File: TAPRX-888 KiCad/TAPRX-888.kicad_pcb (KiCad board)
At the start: 6 copper layers, 76 x 100 mm, 214 parts, among them J1 CONN_SMA_JACK_RA, J10 U.FL-R, J2 CONN_SMA_JACK_RA, J3 CONN_SMA_JACK_RA, J4 CONN_SMA_JACK_RA, J5 USB-3.0, J6 Conn_01x03, J7 Conn_01x03, J8 Conn_01x03, J9 Conn_01x03, Q1 PMOS Si2343DS, Q2 MMBT3904, U1 AP2114H-3.3TRG1, U10 XO-19.2MHZ, U11 CYUSB3014-BZXCT, U14 LP5907MFX-3.3, U16 TLV3501, U18 NC7SV157, U19 74LVC2G14, U2 AP2114H-3.3TRG1, U20 Si5351A, U21 NC7SV157, U22 SN65LVDS1, U3 AP2114H-3.3TRG1, U4 LP5907MFX-3.3, U5 UMW AMS1117-1.2, U6 AD8370, U7 TVS-SP3011, U8 LTC2208CUP_PBF, U9 MX25L3233FM2I, X1 TCXO-27M

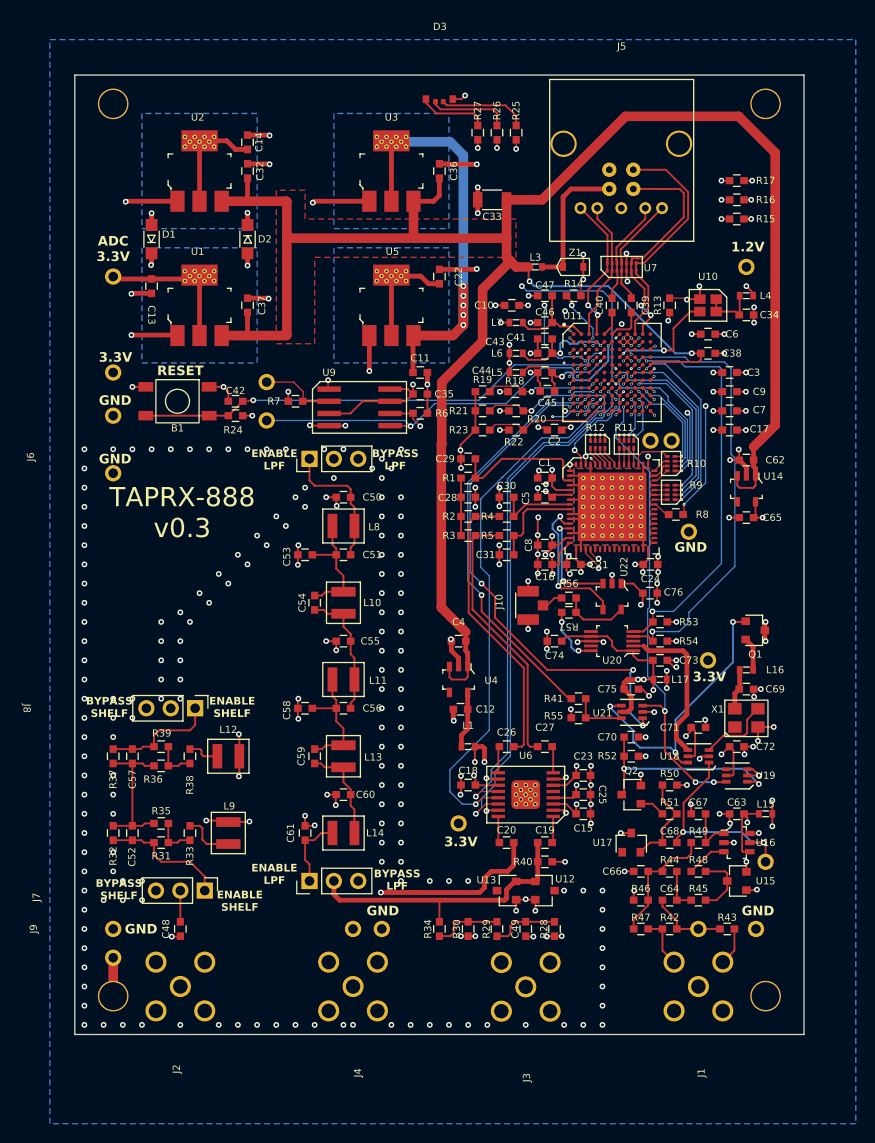
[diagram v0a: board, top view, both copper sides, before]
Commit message: reorg to put into main directory
moved paul's v0.4 work into the main folder
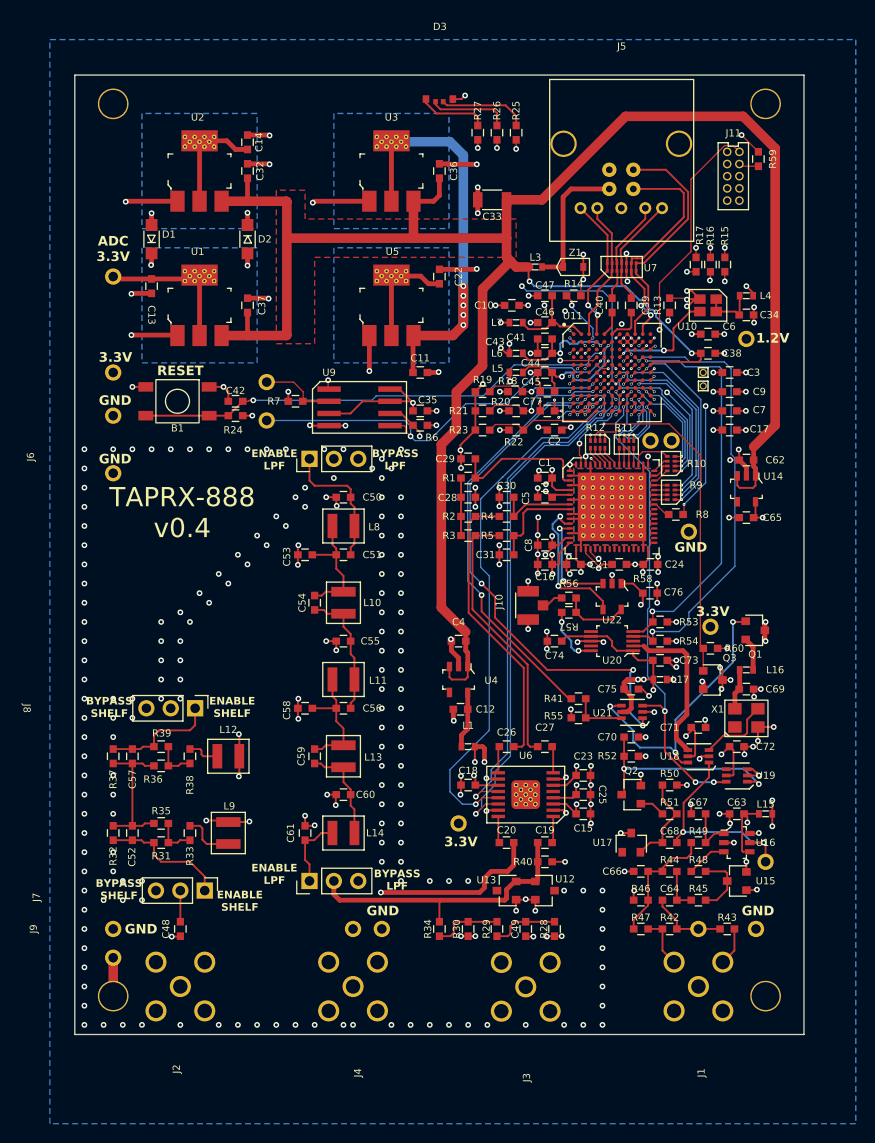
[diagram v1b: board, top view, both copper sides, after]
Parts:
- added C77: C-0.1-0603, TIS_Footprints:C_0603, F.Cu at (149.2, 85.0)
- added J11: Conn_JTAG10-mini, TIS_Footprints:CONN-JTAG10-mini, F.Cu at (168.6, 60.5)
- added Q3: PMOS Si2343DS, TIS_Footprints:SOT-23, F.Cu at (166.5, 113.0)
- added R58: R-47K-0603, TIS_Footprints:PAD_0603, F.Cu at (156.8, 101.0)
- added R59: R-47K-0603, TIS_Footprints:PAD_0603, F.Cu at (171.2, 58.8)
- added R60: R-10K-0603, TIS_Footprints:PAD_0603, F.Cu at (166.2, 109.8)
- added TP20: TP-TINY, TIS_Footprints:TP-Tiny, F.Cu at (165.5, 81.0)
- added TP21: TP-TINY, TIS_Footprints:TP-Tiny, F.Cu at (165.5, 82.4)
- moved R17 9.73 mm to (164.8, 69.8), turned to 90 degrees
- moved TP6 7.50 mm to (170.0, 77.5)
- moved R16 7.29 mm to (166.2, 69.8), turned to 90 degrees
- moved R15 4.91 mm to (167.8, 69.8), turned to 90 degrees
- moved TP17 3.51 mm to (166.2, 107.5)
- moved C35 1.75 mm to (136.0, 85.0)
- moved R6 1.25 mm to (136.0, 86.5)
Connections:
- L17 pad 2: 3V3REF -> /Clock/Vdd5351
- L5 pad 1: +1V2 -> +3V3
- U11 pad B11: unconnected-(U11-TRST-PadB11) -> /TRST
- U11 pad C10: unconnected-(U11-TDO-PadC10) -> /TDO
- U11 pad D3: /ID5 -> unconnected-(U11-GPIO52-PadD3)
- U11 pad E4: unconnected-(U11-GPIO49-PadE4) -> Net-(U11-GPIO49)
- U11 pad E5: unconnected-(U11-GPIO48-PadE5) -> Net-(U11-GPIO48)
- U11 pad E7: unconnected-(U11-TDI-PadE7) -> /TDI
- U11 pad E8: unconnected-(U11-TMS-PadE8) -> /TMS
- U11 pad F4: unconnected-(U11-GPIO41-PadF4) -> /ID5
- U11 pad F6: unconnected-(U11-TCK-PadF6) -> /TCK
- U11 pad J4: unconnected-(U11-GPIO34-PadJ4) -> /DIS_5351
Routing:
- net /DIS_5351: track 0.00 -> 37.2 mm, vias 0 -> 2
- net /TMS: track 0.00 -> 33.7 mm, vias 0 -> 1
- net /RESET_N: track 50.8 -> 81.9 mm, vias 2 -> 3
- net /TRST: track 0.00 -> 28.5 mm, vias 0 -> 1
- net /TDI: track 0.00 -> 27.4 mm, vias 0 -> 1
- net /TCK: track 0.00 -> 27.3 mm, vias 0 -> 1
- net /TDO: track 0.00 -> 23.4 mm, vias 0 -> 1
- net Net-(U11-GPIO49): track 0.00 -> 12.1 mm, vias 0 -> 1
- net +3V3: track 60.8 -> 49.0 mm, vias 23 -> 25
- net Net-(U11-GPIO48): track 0.00 -> 11.1 mm, vias 0 -> 1
- net /ID2: track 28.4 -> 22.4 mm
- net /Clock/Vdd5351: track 0.00 -> 4.62 mm, vias 0 -> 2
- net /ID1: track 28.4 -> 23.8 mm
- net +1V2: track 32.0 -> 29.2 mm, vias 15 -> 17
- net /SPI_MOSI: track 41.0 -> 43.6 mm
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- added copper zone on In3.Cu, net /Clock/CLKGEN3.3V
- added copper zone on In3.Cu, net /Clock/REFCLK3.3V
- added copper zone on In3.Cu, net /VGA3.3V
- added copper zone on In3.Cu, net 3V3REF
- removed copper zone on In2.Cu, net /Clock/CLKGEN3.3V
- removed copper zone on In2.Cu, net /Clock/REFCLK3.3V
- removed copper zone on In2.Cu, net /VGA3.3V
- removed copper zone on In2.Cu, net 3V3REF
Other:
- board text added: "TAPRX-888 v0.4"
- board text removed: "TAPRX-888 v0.3"

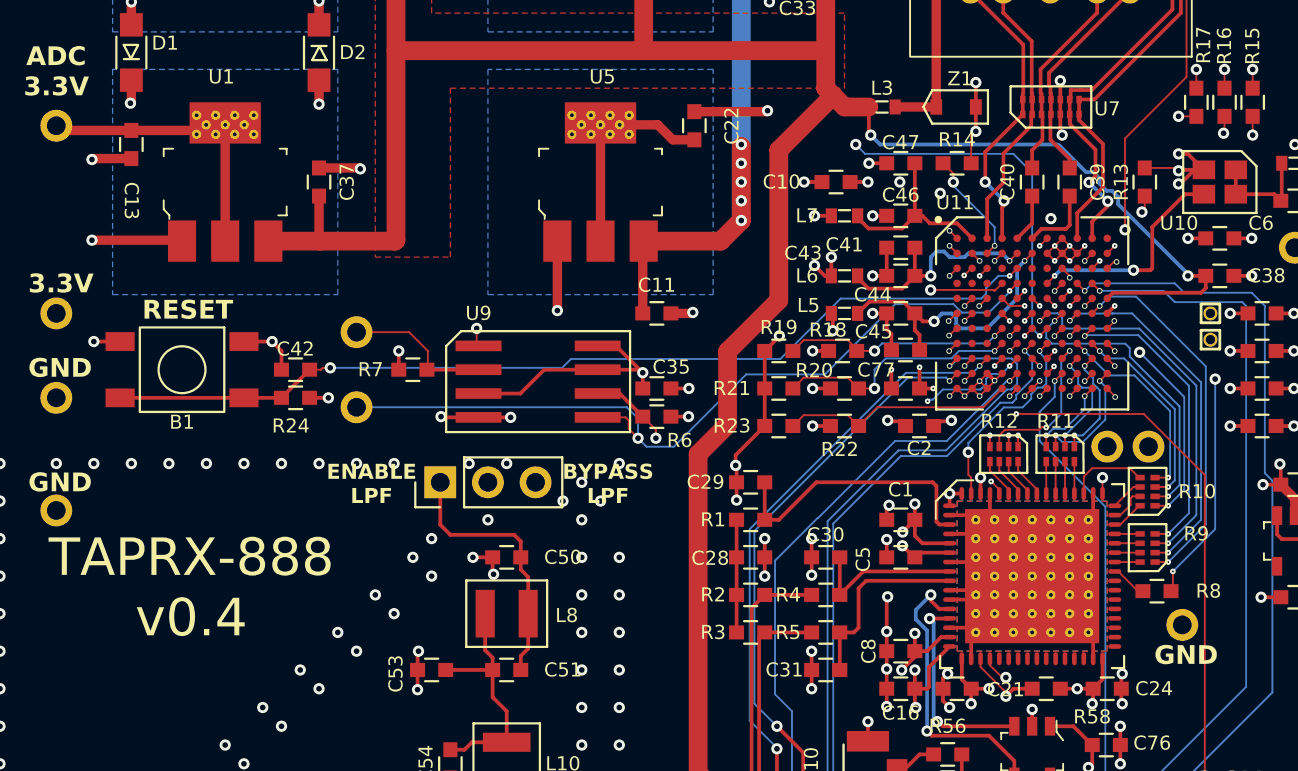
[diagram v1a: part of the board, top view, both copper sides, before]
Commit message: Updated via and relief dimensions
Dimensions based on JLCPCB documentation, but using 0.15mm hole and 0.25mm clearance minimums.
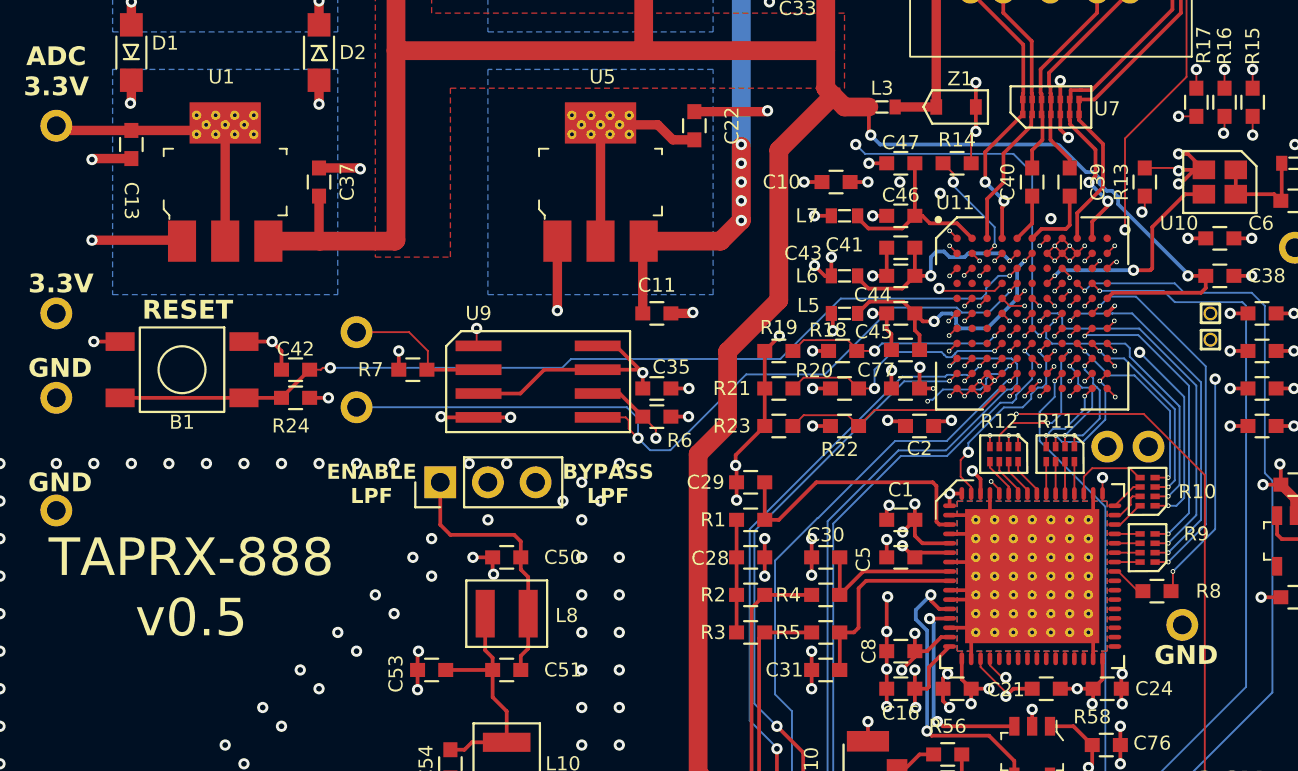
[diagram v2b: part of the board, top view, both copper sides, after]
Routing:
- net +3V3ADC: track 44.9 -> 45.5 mm
- net /DITH: track 24.2 -> 24.7 mm
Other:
- board text added: "TAPRX-888 v0.5"
- board text removed: "TAPRX-888 v0.4"

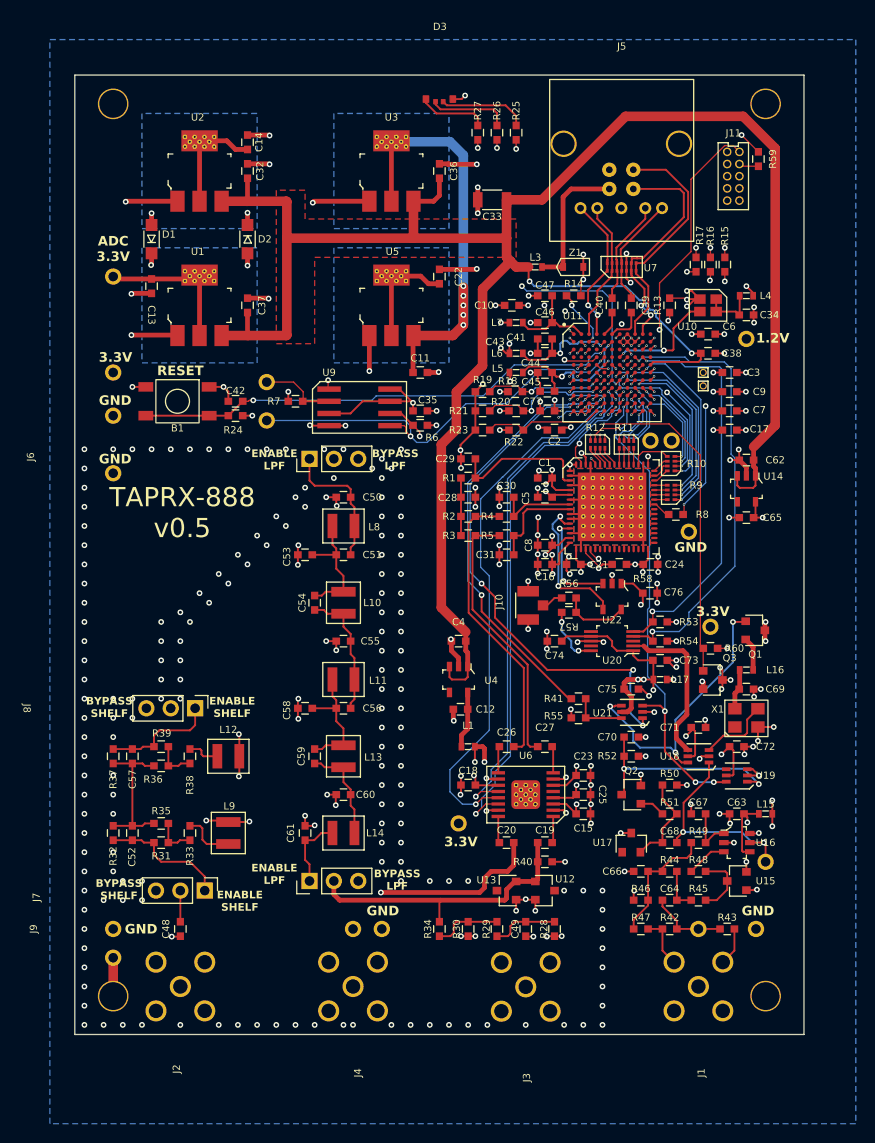
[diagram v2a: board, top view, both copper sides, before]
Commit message: cleanup BGA dimensions
tighter reliefs under BPA, relaxed elsewhere,
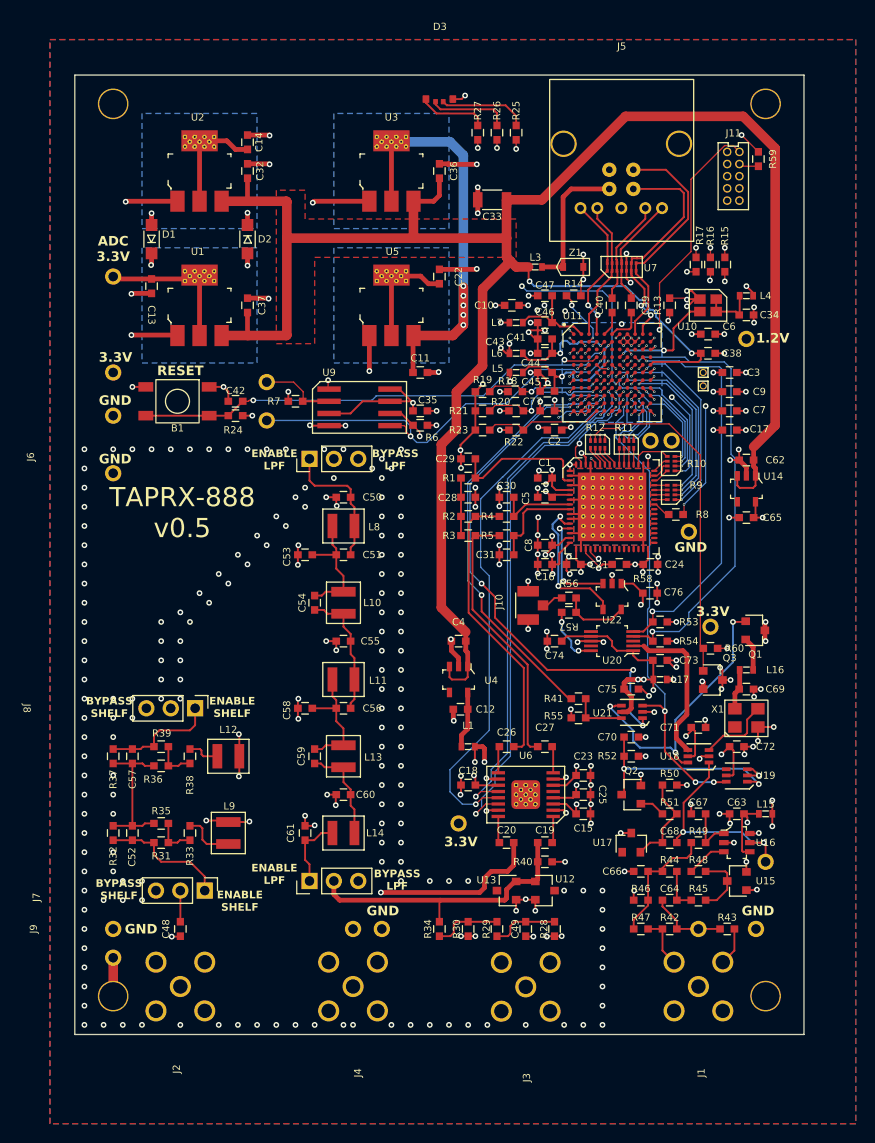
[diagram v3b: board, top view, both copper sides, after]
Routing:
- net GND: track 261.3 -> 268.8 mm, vias 322 -> 326
- net +3V3: track 49.0 -> 49.6 mm
